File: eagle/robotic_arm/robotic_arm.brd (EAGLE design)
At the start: 81.3 x 63.5 mm, 104 parts, among them J2 (ID,OD)=(2.1,5.5)MM, SW1 5A/28V, Y1 16MHz

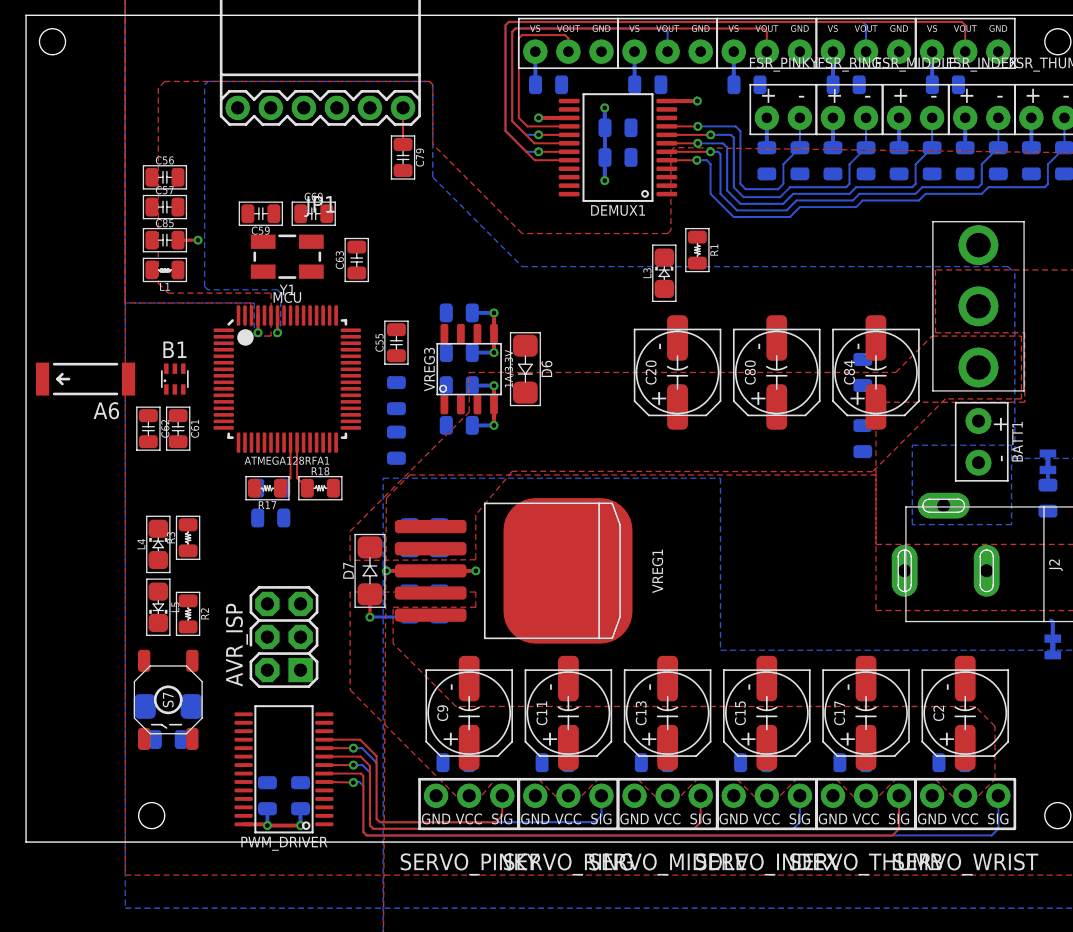
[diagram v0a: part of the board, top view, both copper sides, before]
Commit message: Routed most of VCC.  Rotated PWM Driver to maximize GND plane.  Not sure if the amount of work for this was worth it
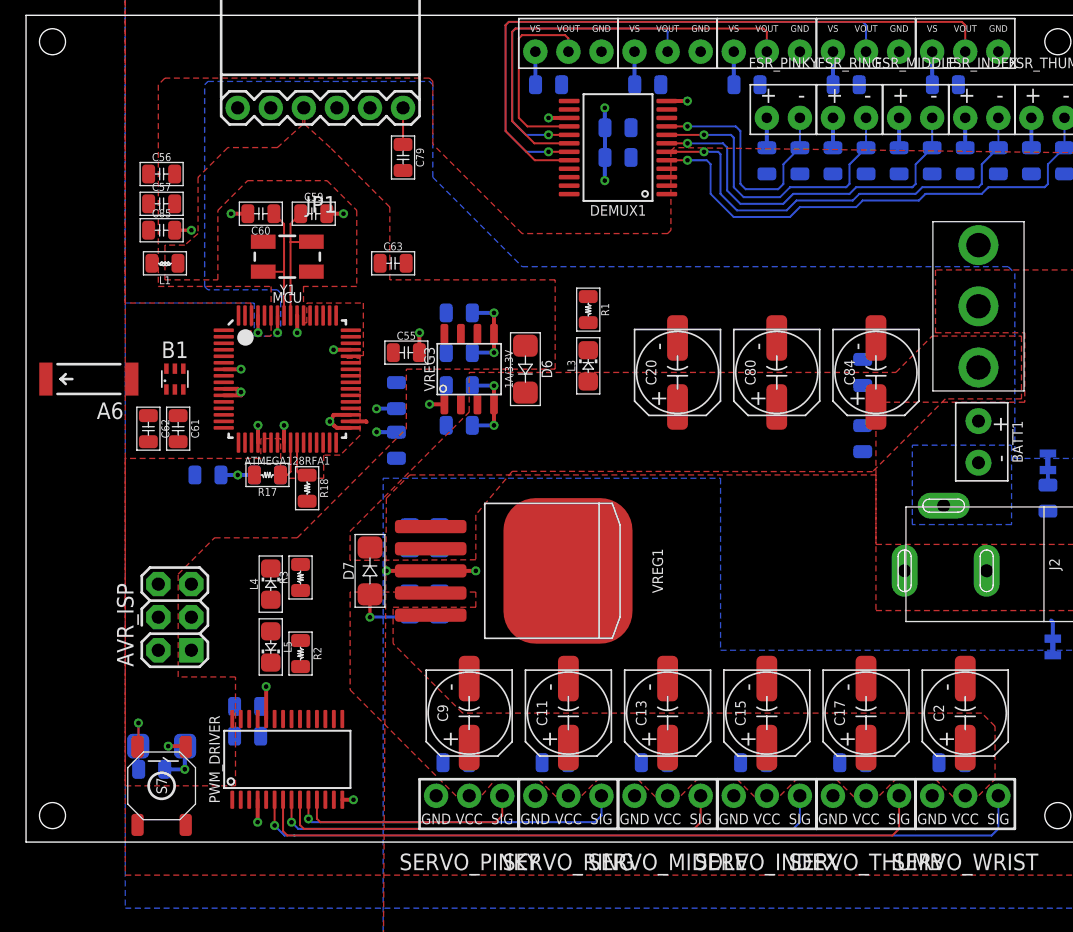
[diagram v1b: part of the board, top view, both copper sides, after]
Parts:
- moved R1 9.55 mm to (45.7, 40.9)
- moved L3 9.20 mm to (45.7, 36.6)
- moved R2 9.16 mm to (23.6, 14.5)
- moved L4 9.16 mm to (21.3, 19.8)
- moved L5 9.16 mm to (21.3, 15.0)
- moved R3 9.16 mm to (23.6, 20.3)
- moved AVR_ISP 8.52 mm to (14.0, 17.3)
- moved C25 7.03 mm to (19.6, 10.4), turned to 180 degrees
- moved S7 6.62 mm to (13.0, 4.32), turned to 270 degrees
- moved C19 6.12 mm to (19.6, 8.13), turned to 180 degrees
- moved C52 4.93 mm to (16.5, 28.2), turned to 0 degrees
- moved C59 4.06 mm to (24.6, 48.3), turned to 0 degrees
- moved C60 4.06 mm to (20.6, 48.3), turned to 180 degrees
- moved C58 3.31 mm to (21.1, 28.2)
- moved D1 3.09 mm to (13.0, 7.37), turned to 180 degrees
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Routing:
- net GND: track 1.45 -> 26.3 mm, vias 0 -> 15
- net N$35: track 0.00 -> 9.75 mm
- net N$30: track 0.00 -> 9.74 mm
- net RESET: track 0.00 -> 5.59 mm, vias 0 -> 1
- net SERVO_WRIST: track 20.9 -> 17.5 mm
- net VCC: track 13.4 -> 16.6 mm, vias 4 -> 6
- net SERVO_PINKY: track 58.3 -> 60.7 mm
- net SERVO_THUMB: track 27.9 -> 25.8 mm
- net AGND: track 9.01 -> 7.23 mm
- net SERVO_RING: track 51.4 -> 52.6 mm
- net SERVO_INDEX: track 36.1 -> 35.1 mm
- net SDA: track 3.83 -> 3.11 mm
- added copper zone on layer 1, net VCC

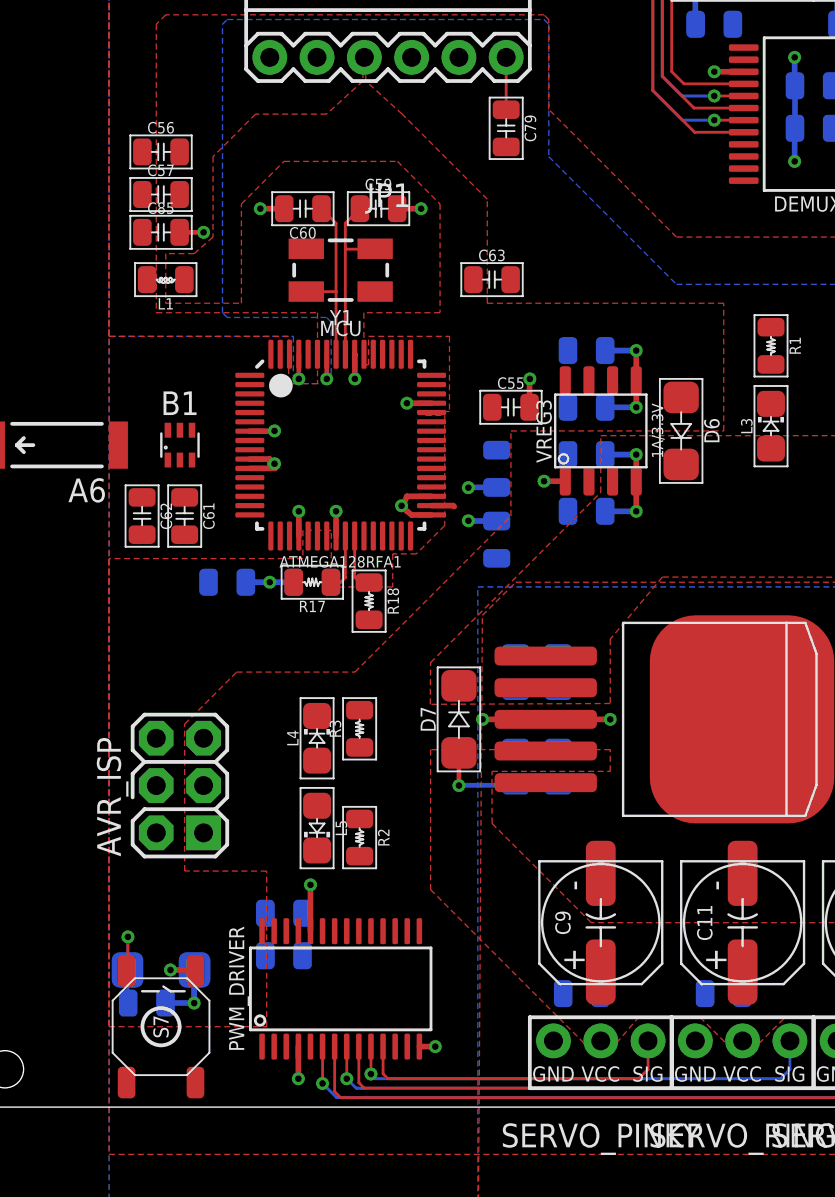
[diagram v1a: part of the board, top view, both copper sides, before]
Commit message: Slight tweaks to last routing of VCC and some of the passive components around it.
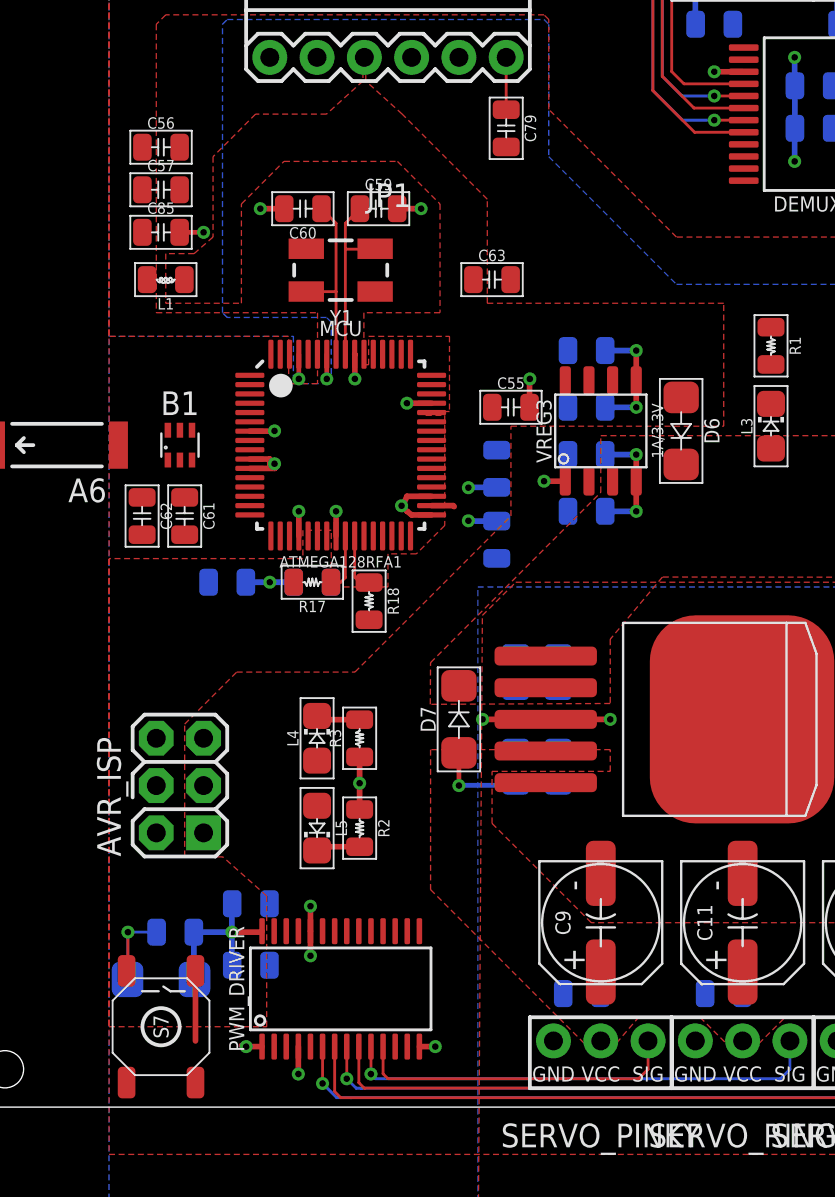
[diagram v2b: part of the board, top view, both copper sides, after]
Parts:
- moved R43 4.10 mm to (13.7, 9.40)
- moved C25 1.85 mm to (17.8, 10.9)
- moved C19 1.85 mm to (17.8, 7.62)
- moved R2 0.51 mm to (23.6, 15.0)
- moved D1 0.51 mm to (13.0, 6.86)
- moved R3 0.51 mm to (23.6, 19.8)
- moved C57 0.25 mm to (13.0, 49.3)
- moved C56 0.25 mm to (13.0, 51.6)
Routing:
- net GND: track 26.3 -> 32.7 mm, vias 15 -> 17
- net VCC: track 16.6 -> 22.8 mm
- net N$5: track 0.00 -> 2.37 mm
- net N$3: track 0.00 -> 2.37 mm
- net RESET: track 5.59 -> 6.19 mm

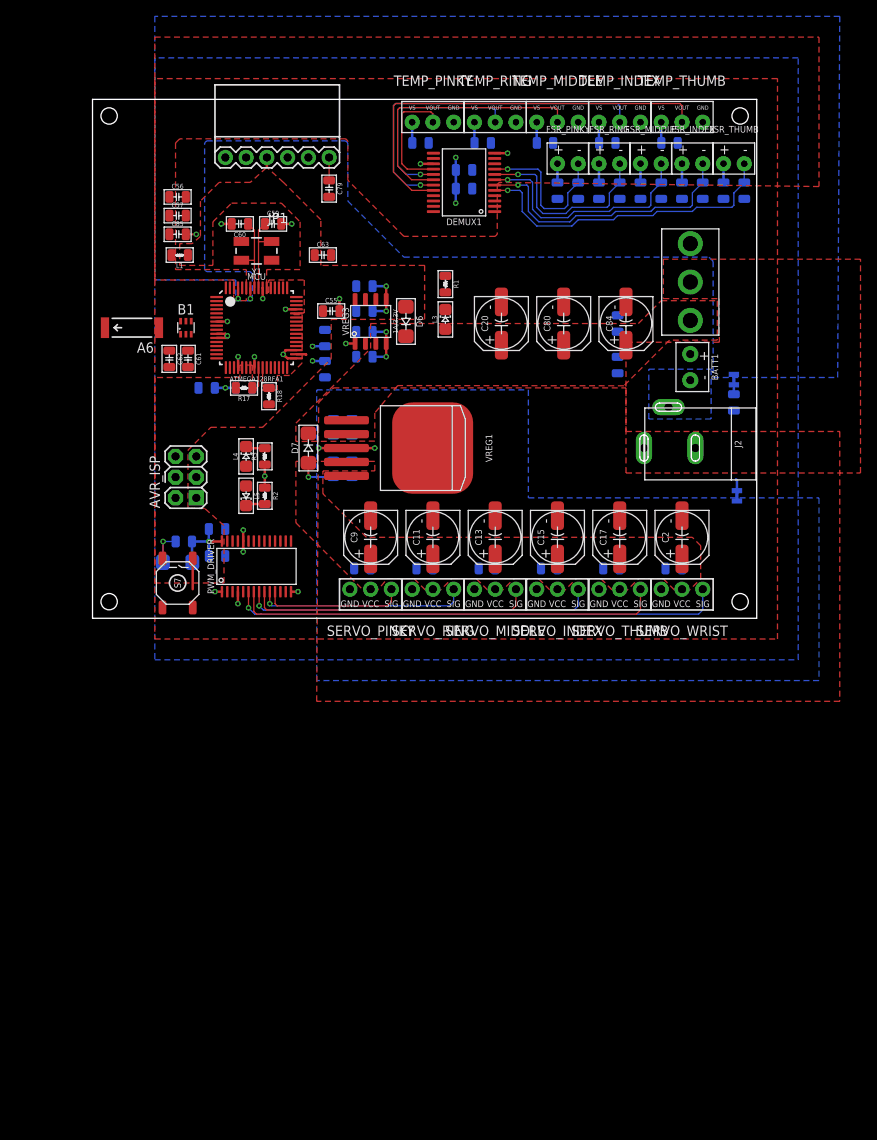
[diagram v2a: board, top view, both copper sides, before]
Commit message: Fucked up.  Forgot pull down and current limiting resistors on PWM driver to servosgit add -A  Added them.  Need to increase size of board and reroute
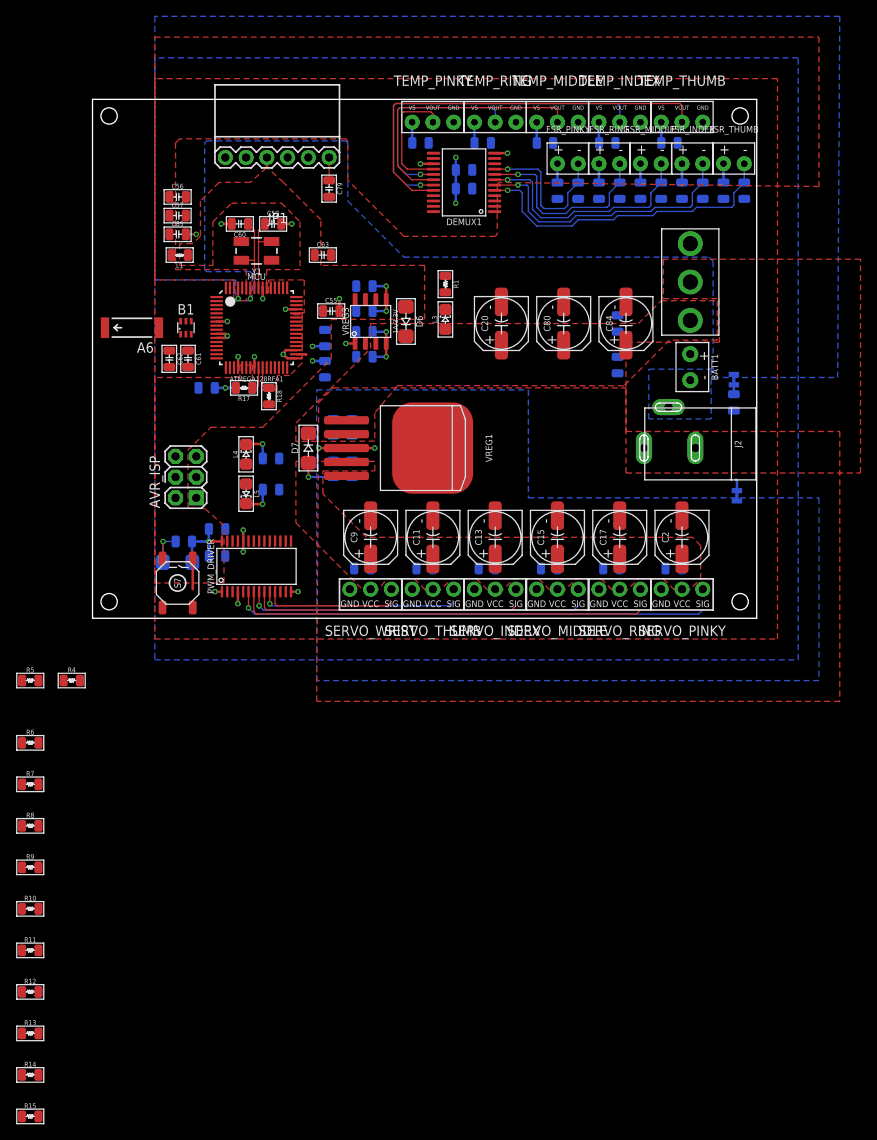
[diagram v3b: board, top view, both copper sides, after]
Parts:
- added R10, R12, R14, R4, R6, R8: 10KΩ, MrSwirlyEyes:RESISTOR_SMD-805
- added R11, R13, R15, R5, R7, R9: 100Ω, MrSwirlyEyes:RESISTOR_SMD-805
- moved SERVO_PINKY 38.1 mm to (74.7, 2.29)
- moved SERVO_WRIST 38.1 mm to (36.6, 2.29)
- moved SERVO_RING 22.9 mm to (67.1, 2.29)
- moved SERVO_THUMB 22.9 mm to (44.2, 2.29)
- moved SERVO_INDEX 7.62 mm to (51.8, 2.29)
- moved SERVO_MIDDLE 7.62 mm to (59.4, 2.29)
- moved R2 1.08 mm to (24.4, 15.7), flipped to the bottom, turned to 0 degrees
- moved R3 0.80 mm to (24.4, 19.6), flipped to the bottom, turned to 0 degrees
- moved L5 0.25 mm to (21.3, 15.2)
- moved L4 0.25 mm to (21.3, 20.1)
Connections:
- new net N$1: R11.1, SERVO_WRIST.1
- new net N$4: R9.1, SERVO_THUMB.1
- new net N$6: R7.1, SERVO_INDEX.1
- new net N$7: R5.1, SERVO_MIDDLE.1
- new net N$8: R15.1, SERVO_RING.1
- new net N$9: R13.1, SERVO_PINKY.1
- net GND: now also R10.1, R12.1, R14.1, R4.1, R6.1, R8.1
- net SERVO_INDEX: now also R6.2, R7.2; no longer SERVO_MIDDLE.1
- net SERVO_MIDDLE: now also R4.2, R5.2; no longer SERVO_INDEX.1
- net SERVO_PINKY: now also R12.2, R13.2; no longer SERVO_WRIST.1
- net SERVO_RING: now also R14.2, R15.2; no longer SERVO_THUMB.1
- net SERVO_THUMB: now also R8.2, R9.2; no longer SERVO_RING.1
- net SERVO_WRIST: now also R10.2, R11.2; no longer SERVO_PINKY.1
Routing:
- net GND: track 32.7 -> 29.9 mm, vias 17 -> 16
- net SERVO_RING: track 52.6 -> 50.1 mm
- net SERVO_PINKY: track 60.7 -> 58.2 mm
- net SERVO_MIDDLE: track 43.3 -> 41.3 mm
- net SERVO_INDEX: track 35.1 -> 33.0 mm
- net SERVO_WRIST: track 17.5 -> 16.0 mm
- net SERVO_THUMB: track 25.8 -> 24.3 mm
- net N$3: track 2.37 -> 3.85 mm, vias 0 -> 1
- net N$5: track 2.37 -> 3.85 mm, vias 0 -> 1

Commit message: Fixed mistake and added the resistors needed for PWM driver and servos.  Increased board width, bringing board coast to 1.60.  Rerouted PWM driver and servos with respective resistors
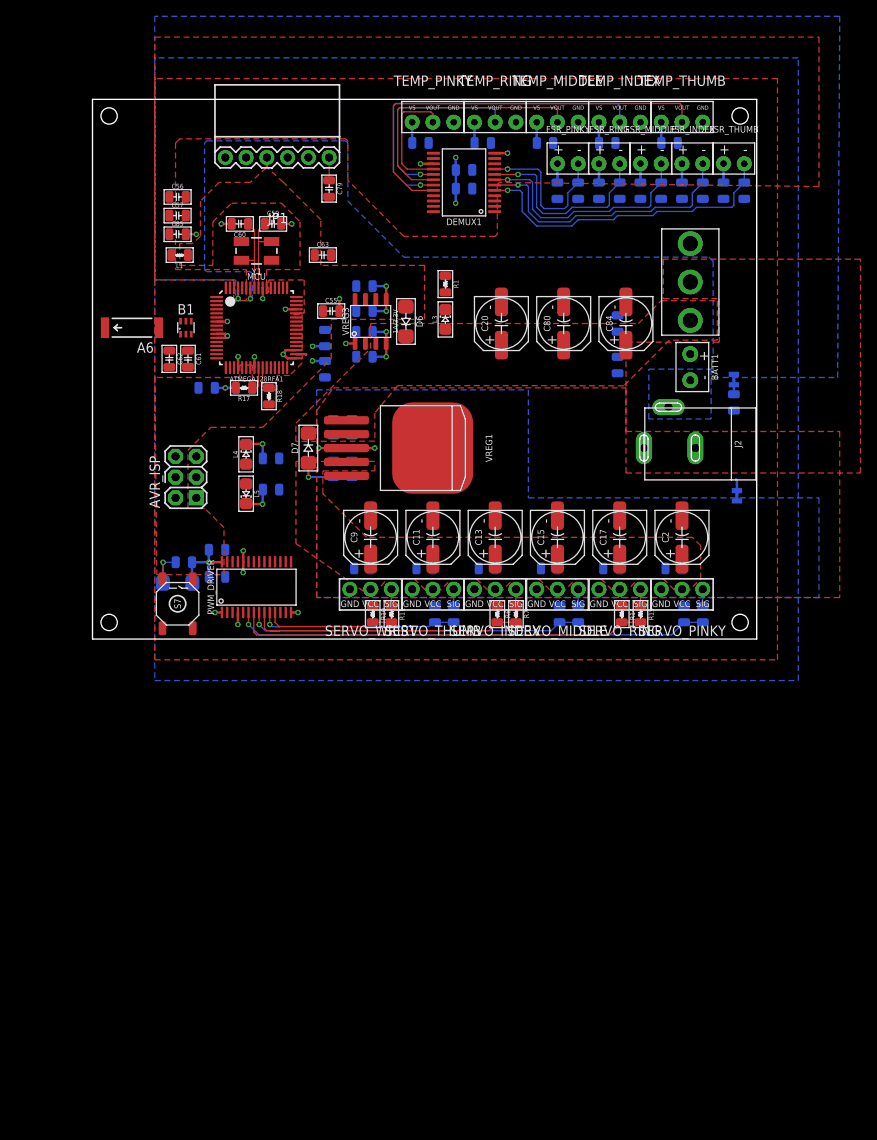
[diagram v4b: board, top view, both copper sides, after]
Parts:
- moved R13 97.0 mm to (77.2, 0.51), flipped to the bottom, turned to 270 degrees
- moved R15 96.7 mm to (69.6, 0.51), turned to 270 degrees
- moved R12 92.4 mm to (74.9, 0.51), flipped to the bottom, turned to 270 degrees
- moved R14 91.8 mm to (67.3, 0.51), turned to 270 degrees
- moved R5 67.5 mm to (62.0, 0.51), flipped to the bottom, turned to 270 degrees
- moved R7 63.0 mm to (54.4, 0.51), turned to 270 degrees
- moved R11 60.4 mm to (39.1, 0.51), turned to 270 degrees
- moved R9 60.4 mm to (46.7, 0.51), flipped to the bottom, turned to 270 degrees
- moved R4 60.2 mm to (59.7, 0.51), flipped to the bottom, turned to 270 degrees
- moved R6 59.3 mm to (52.1, 0.51), turned to 270 degrees
- moved R8 55.9 mm to (44.5, 0.51), flipped to the bottom, turned to 270 degrees
- moved R10 55.3 mm to (36.8, 0.51), turned to 270 degrees
- moved C25 2.54 mm to (17.8, 8.38)
- moved C19 2.54 mm to (17.8, 5.08)
- moved D1 2.54 mm to (13.0, 4.32)
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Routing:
- net GND: track 29.9 -> 26.1 mm
- net N$9: track 0.00 -> 2.05 mm
- net N$8: track 0.00 -> 2.05 mm
- net N$7: track 0.00 -> 2.05 mm
- net N$6: track 0.00 -> 2.05 mm
- net N$4: track 0.00 -> 2.05 mm
- net N$1: track 0.00 -> 2.05 mm
- net SERVO_MIDDLE: track 41.3 -> 42.5 mm
- net SERVO_WRIST: track 16.0 -> 16.6 mm
- net SERVO_THUMB: track 24.3 -> 24.8 mm
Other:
- board size 81.3 x 63.5 mm -> 81.3 x 66 mm

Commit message: Slight tweaks to power planes and general routing of top and bottom of the board
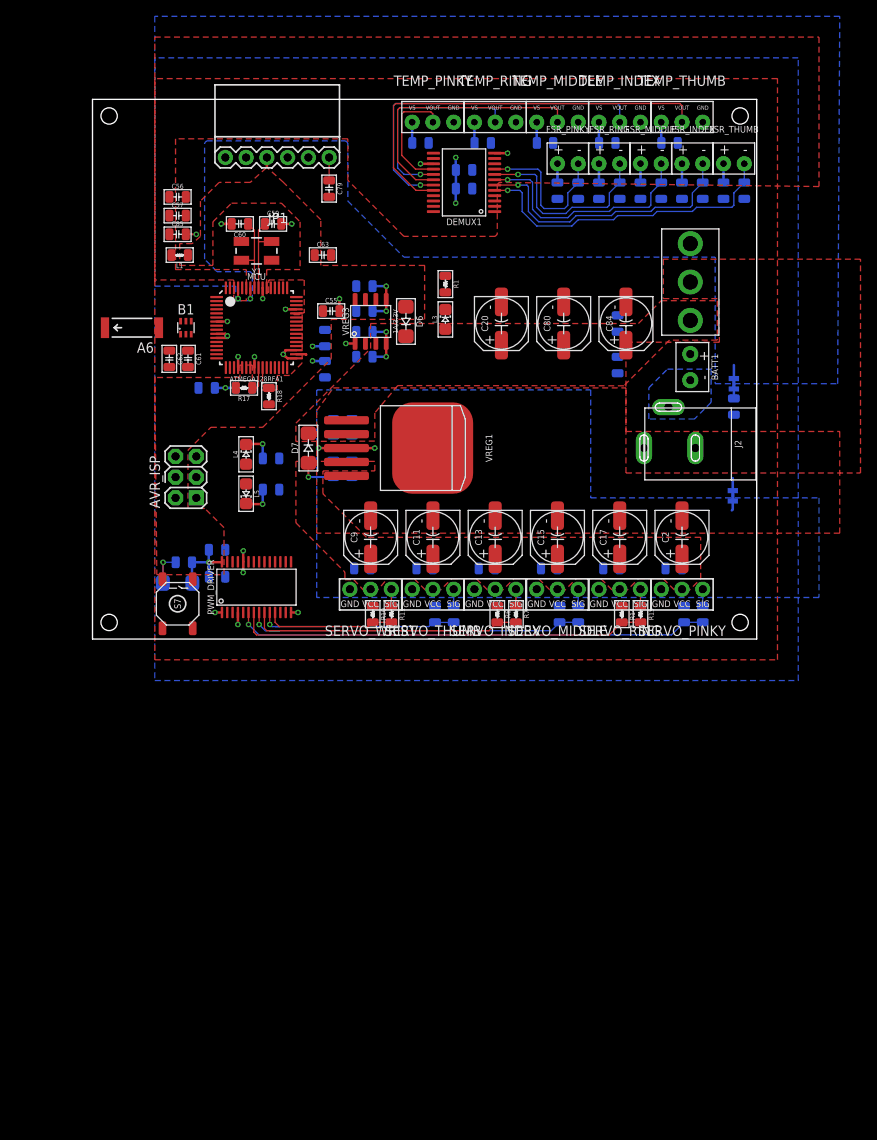
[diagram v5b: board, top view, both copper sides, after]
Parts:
- moved SUPPLY51 0.51 mm to (80.9, 15.0)
- moved L2 0.51 mm to (81.0, 25.9)
- moved SUPPLY52 0.51 mm to (81.0, 28.7)
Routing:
- net AGND: track 7.23 -> 8.88 mm
- net NGND: track 6.86 -> 8.05 mm
- net TEMP_THUMB: track 15.3 -> 14.7 mm
